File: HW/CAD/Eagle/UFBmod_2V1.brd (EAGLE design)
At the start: 98.4 x 89.5 mm, 197 parts, among them T0551 MMBT2222, U0501 MIDAS_MCCOG21605B6W-FPTLWI, U0601 MAX5217, U0701 AT86RF215-ZU, U0711 ASVTX-13-D-26.000MHZ-I05-T, U0811 PE4259, U0821 RFX1010, U0881 B39871B3440U410, U0911 FT232HL, U1101 TPS53353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

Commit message: HW_2V0 - CAD/Eagle - USB ETH and RX/TX imp lines routed
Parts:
- moved L0821 1.59 mm to (16.2, 67.3), turned to 180 degrees
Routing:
- net FPGA_ETH_RD_P: track 41.1 -> 46.7 mm, vias 3 -> 1
- net FPGA_ETH_RD_N: track 40.4 -> 45.7 mm, vias 3 -> 1
- net USB_D_P: track 38.5 -> 36.9 mm
- net ANT24: track 6.84 -> 7.79 mm, vias 0 -> 1
- net USB_D_N: track 38.6 -> 37.7 mm
- net FE09_ANT: track 4.46 -> 5.26 mm
- net FPGA_ETH_TD_P: track 41.5 -> 42.1 mm, vias 3 -> 1
- net FPGA_ETH_TD_N: track 41.1 -> 41.5 mm, vias 3 -> 1
- added copper zone on layer 1, net TRX_AVSS
- added copper zone on layer 3, net TRX_AVSS

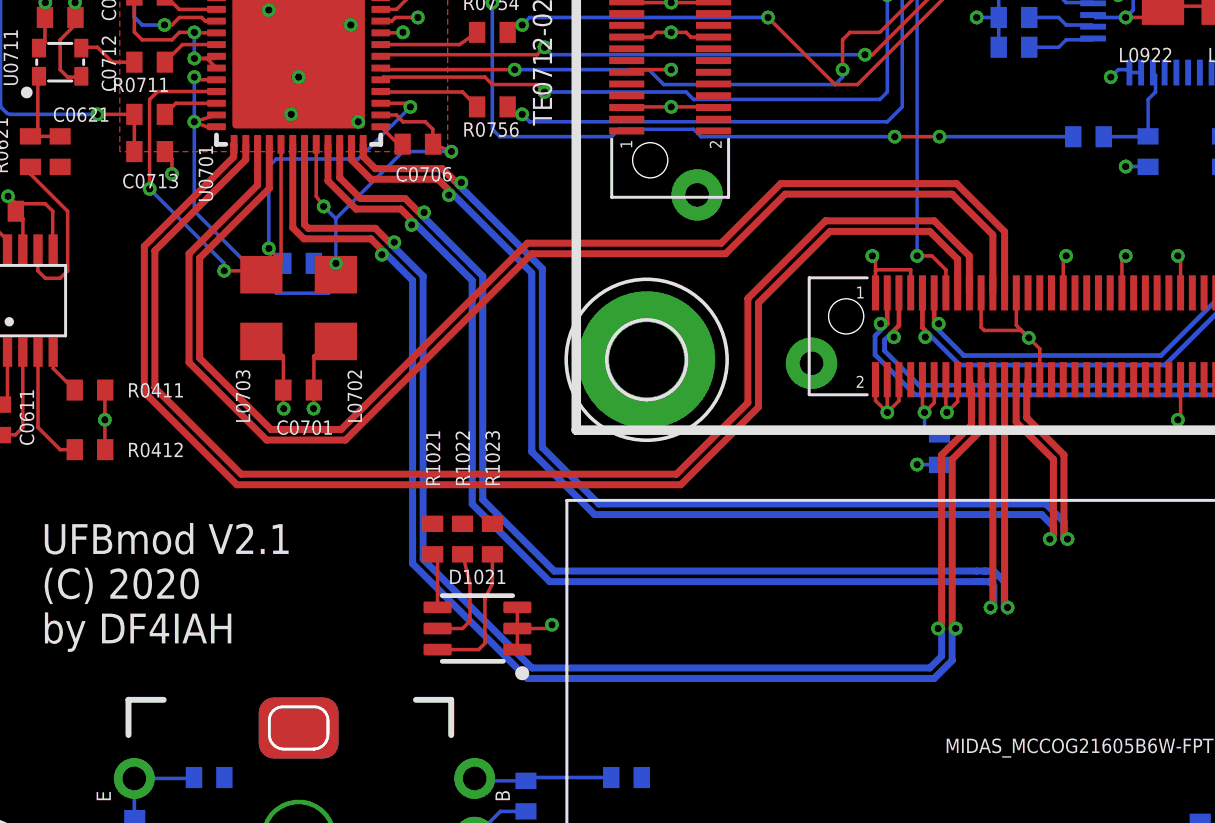
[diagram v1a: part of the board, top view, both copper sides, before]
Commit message: HW_2V0 - CAD/Eagle - LVDS imp lines routed
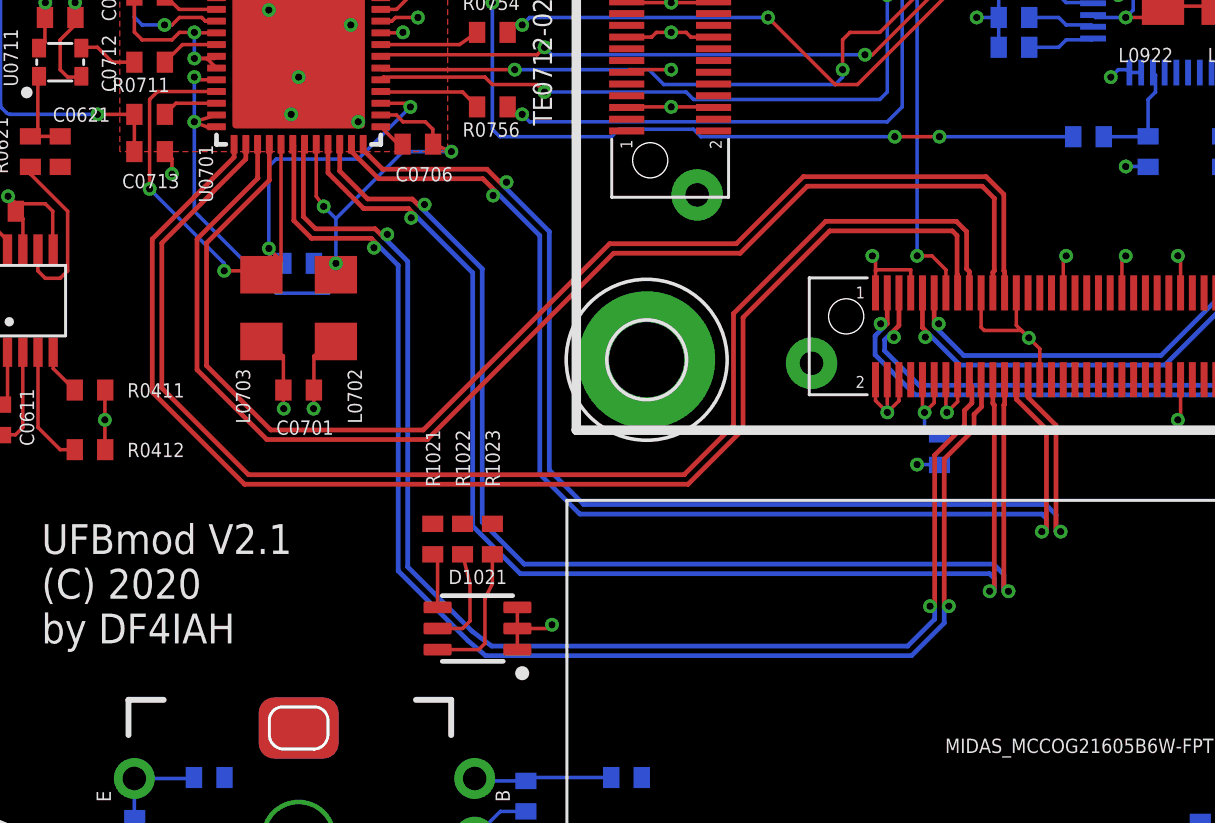
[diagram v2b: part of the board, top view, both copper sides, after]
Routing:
- net TRX_RXD09_N: track 60.1 -> 58.6 mm
- net TRX_RXD09_P: track 58.6 -> 57.3 mm
- net TRX_TXD_N: track 53.7 -> 54.6 mm
- net TRX_TXD_P: track 53.7 -> 54.6 mm
- net TRX_RXD24_N: track 50.1 -> 50.7 mm
- net TRX_RXD24_P: track 50.1 -> 50.6 mm

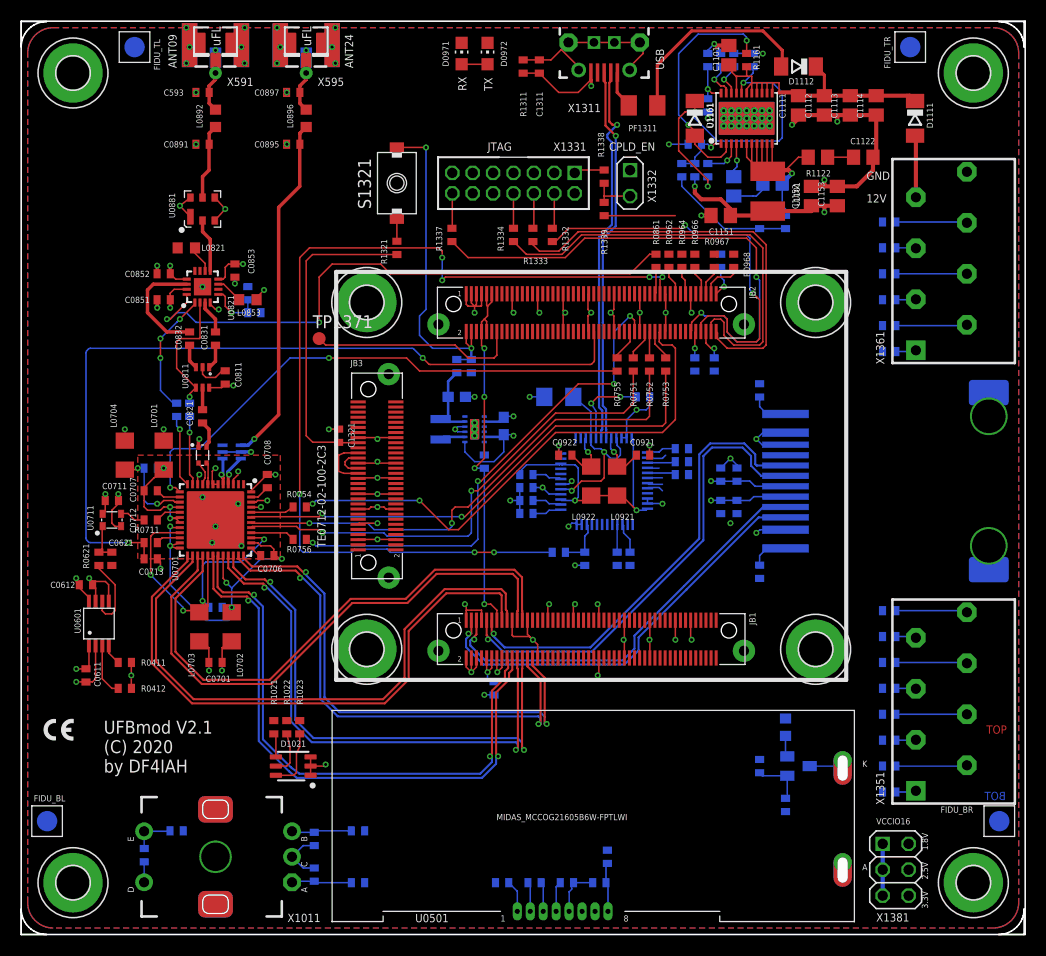
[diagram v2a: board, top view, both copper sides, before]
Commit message: HW_2V1 - CAD/Eagle - multiple nets routed
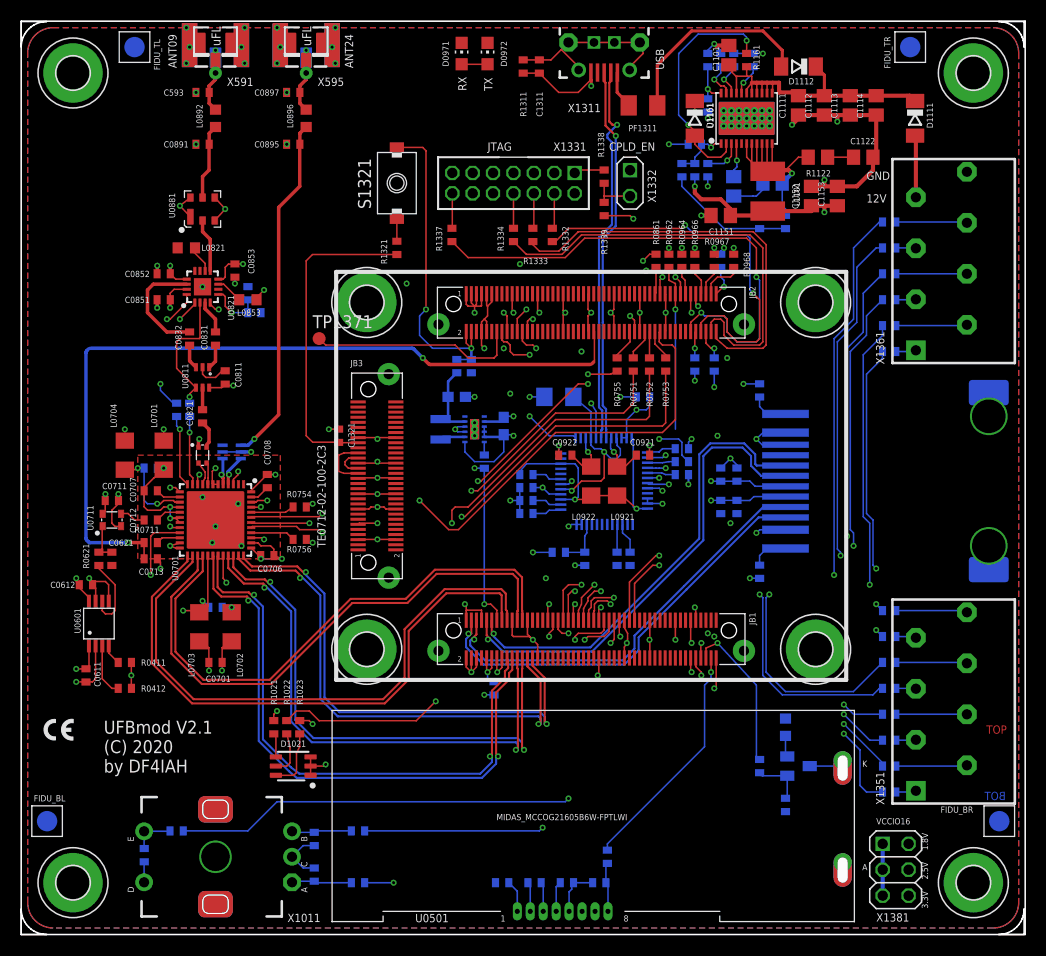
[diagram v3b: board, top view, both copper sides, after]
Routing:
- net BOARD_ROTENC_PUSH: track 0.00 -> 89.7 mm, vias 0 -> 2
- net FPGA_B16_L9_N: track 0.00 -> 69.5 mm, vias 0 -> 2
- net BOARD_ROTENC_I: track 0.00 -> 68.8 mm, vias 0 -> 2
- net BOARD_ROTENC_Q: track 0.00 -> 68.5 mm, vias 0 -> 2
- net FPGA_B16_L9_P: track 0.00 -> 64.9 mm, vias 0 -> 2
- net FPGA_B16_L11_N: track 0.00 -> 61.2 mm, vias 0 -> 2
- net FPGA_B16_L7_N: track 0.00 -> 59.5 mm, vias 0 -> 3
- net FPGA_B16_L11_P: track 0.00 -> 58.5 mm, vias 0 -> 2
- net FPGA_B16_L7_P: track 0.00 -> 56.2 mm, vias 0 -> 3
- net FPGA_ETH_DA_Y: track 0.00 -> 48.8 mm, vias 0 -> 3
- net FPGA_LED_RGB_GREEN: track 0.00 -> 46.7 mm, vias 0 -> 2
- net FPGA_LED_RGB_BLUE: track 0.00 -> 46.1 mm, vias 0 -> 2
- net FPGA_LED_RGB_RED: track 0.00 -> 46.0 mm, vias 0 -> 2
- net FPGA_JTAGEN: track 6.97 -> 51.8 mm, vias 0 -> 2
- net FPGA_B16_L19_N: track 0.00 -> 43.3 mm, vias 0 -> 2
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
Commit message: HW_2V1 - CAD/Eagle - initial routing done, ERC and DRC to follow
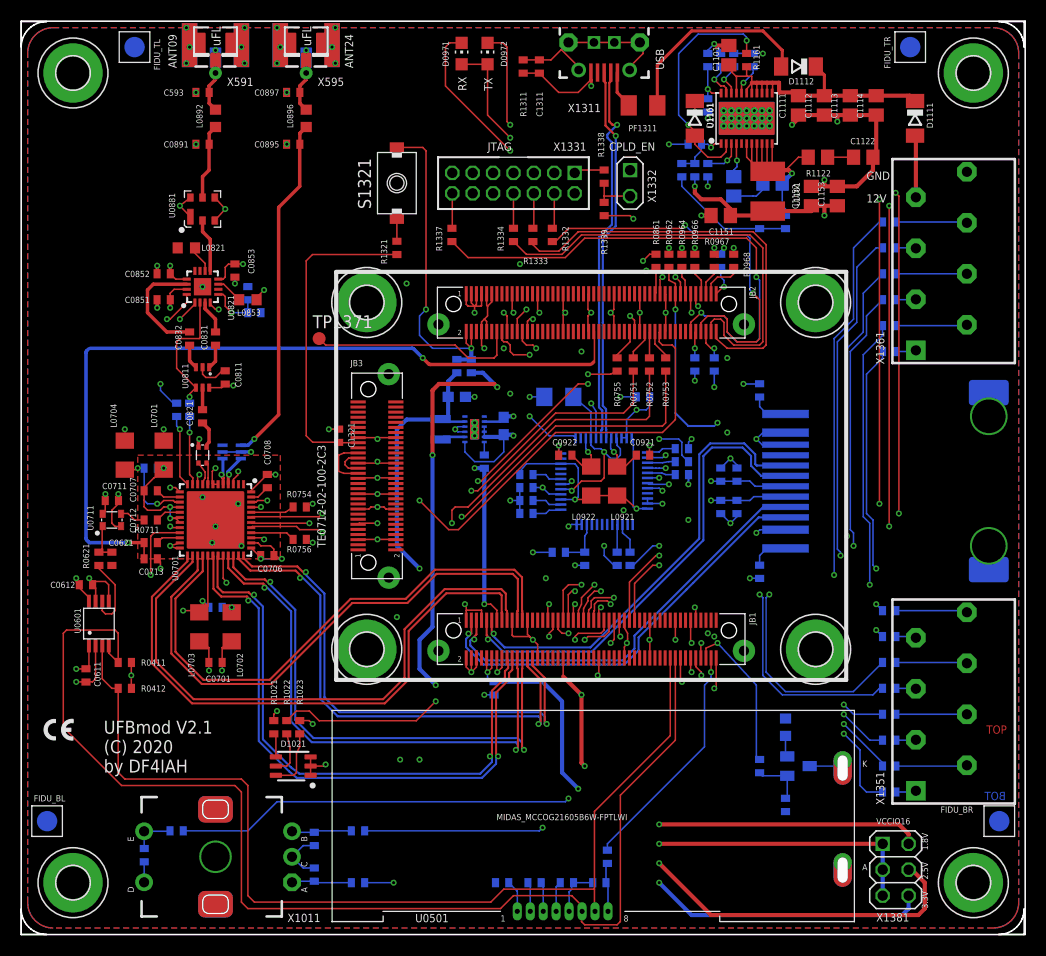
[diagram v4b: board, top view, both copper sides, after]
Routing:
- net BOARD_SDA: track 2.04 -> 119.0 mm
- net FT_TXLED_D: track 0.00 -> 115.7 mm, vias 0 -> 4
- net FT_RXLED_D: track 0.00 -> 113.3 mm, vias 0 -> 4
- net FT_VCCD: track 28.7 -> 130.4 mm, vias 2 -> 5
- net U1V8: track 0.00 -> 101.6 mm, vias 0 -> 6
- net +2V5: track 8.26 -> 107.0 mm, vias 0 -> 3
- net BOARD_SCL: track 5.21 -> 100.2 mm
- net U3V3: track 37.3 -> 118.7 mm, vias 3 -> 6
- net VCCIO16: track 9.47 -> 58.2 mm, vias 1 -> 3
- net FPGA_UART0_TXD: track 16.3 -> 58.7 mm, vias 1 -> 5
- net GND: track 237.8 -> 240.4 mm
- net FPGA_UART0_RXD: track 23.1 -> 24.7 mm

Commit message: HW_2V1 - CAD/Eagle - ERC done
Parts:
- added R0203: 10kR, df4iah_rcl:R0402
- added TP_EN1, TP_MODE, TP_PGOOD, TP_RESIN, TP_RFX_DET, TP_TXDEN: TPB1,27, df4iah_connector:B1,27
- J1411: value (none) -> ABRACON_ARJE-0034
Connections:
- new net FPGA_EN1: JB1.27, TP_EN1.TP
- new net FPGA_MODE: JB1.31, TP_MODE.TP
- new net PGOOD: JB1.29, TP_PGOOD.TP
- new net RESIN: JB2.17, R0203.1, TP_RESIN.TP
- net +3V3: now also R0203.2
- net FPGA_RFX_DET: now also TP_RFX_DET.TP
- net FT_TXDEN: now also TP_TXDEN.TP
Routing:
- net FPGA_MODE: track 0.00 -> 35.2 mm, vias 0 -> 2
- net PGOOD: track 0.00 -> 28.5 mm, vias 0 -> 2
- net FT_TXDEN: track 0.00 -> 25.7 mm, vias 0 -> 1
- net FPGA_EN1: track 0.00 -> 25.3 mm, vias 0 -> 2
- net RESIN: track 0.00 -> 4.49 mm
- net FPGA_RFX_DET: track 0.00 -> 2.97 mm, vias 0 -> 1
- net +3V3: track 95.5 -> 97.8 mm
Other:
- board text added: "TP EN1"
- board text added: "TP MODE"
- board text added: "TP PGOOD"
- board text added: "TP TXDEN"

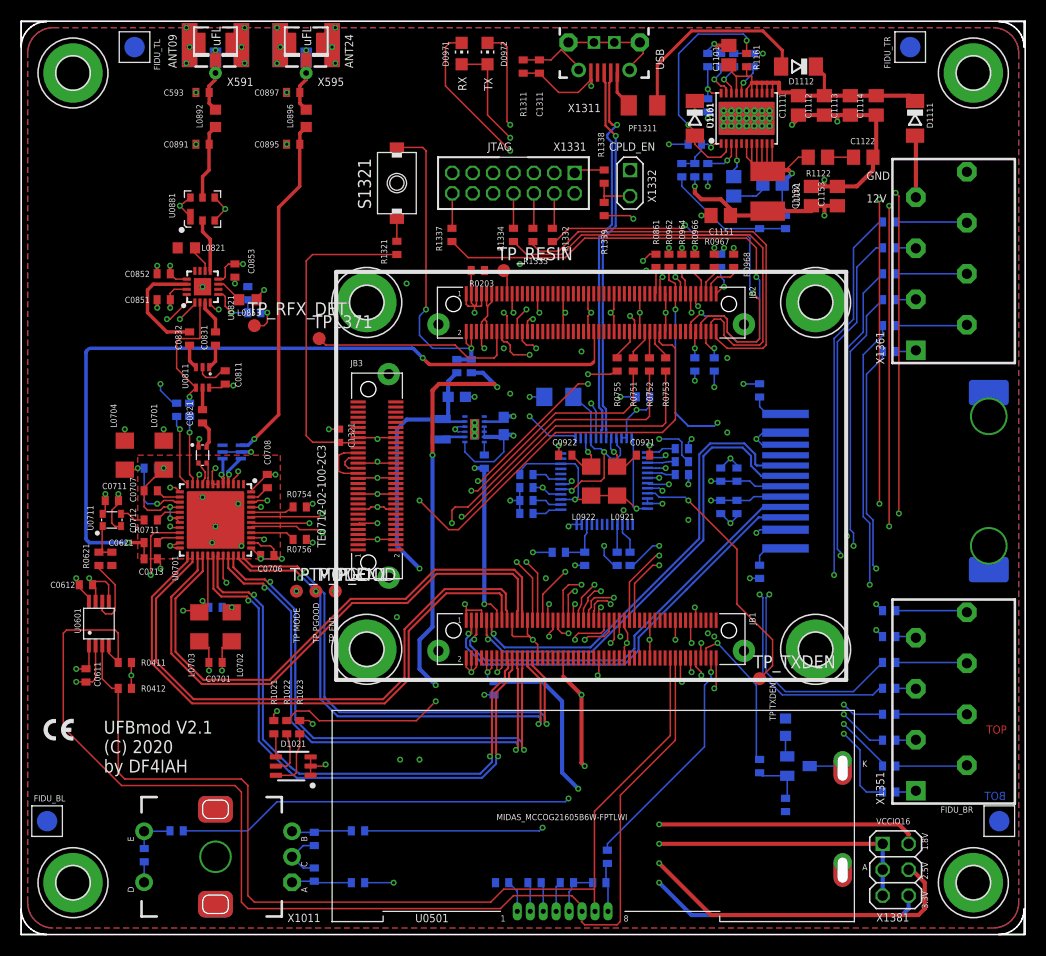
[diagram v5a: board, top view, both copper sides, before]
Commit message: HW_2V1 - CAD/Eagle - DRC work-of-the-day
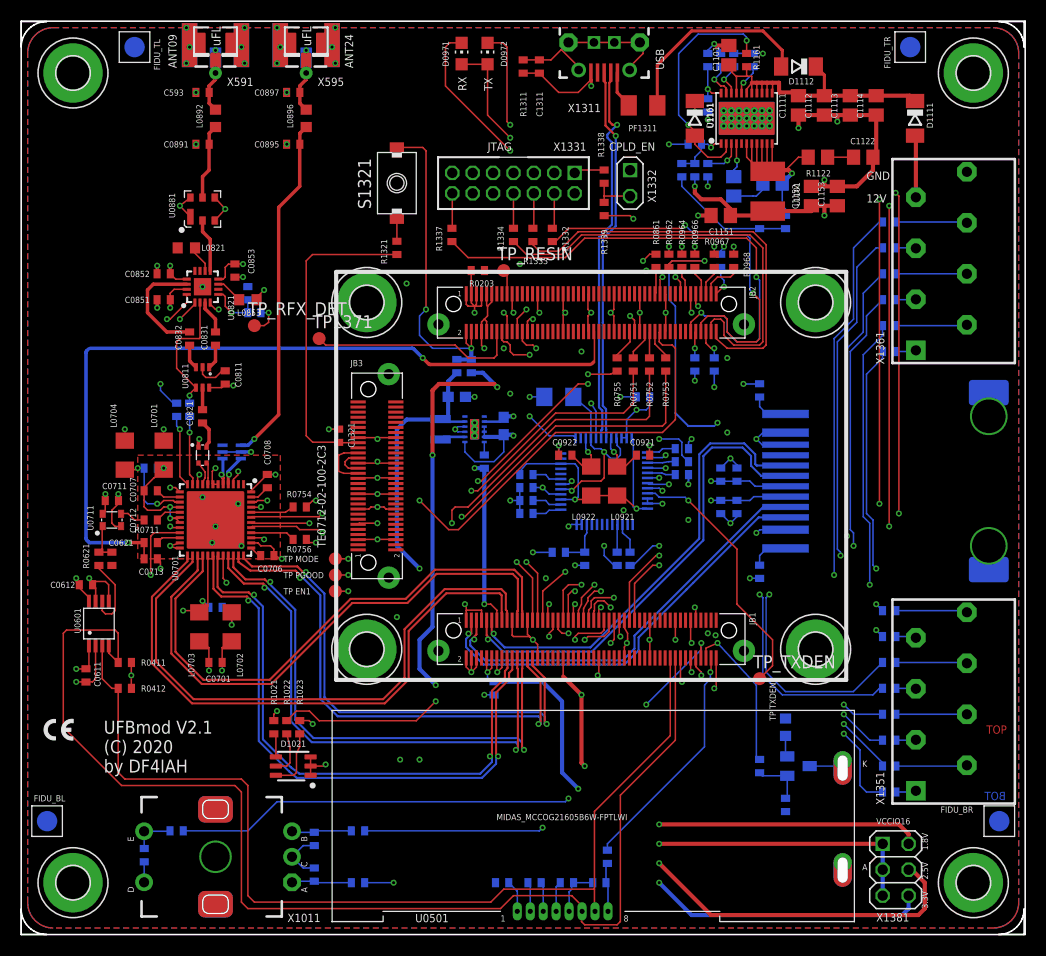
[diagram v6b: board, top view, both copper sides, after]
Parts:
- removed TP_MODE, TP_PGOOD: TPB1,27, df4iah_connector:B1,27
- added FPGA_MODE, PGOOD: TPB1,27, df4iah_connector:B1,27
- renumbered TP_EN1 to FPGA_EN1
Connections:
- net FPGA_MODE: now also FPGA_MODE.TP; no longer TP_MODE.TP
- net PGOOD: now also PGOOD.TP; no longer TP_PGOOD.TP
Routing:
- net FPGA_UART0_TXD: track 58.7 -> 66.5 mm
- net TRX_DVSS: track 34.1 -> 37.0 mm, vias 6 -> 5
- net FPGA_EN1: track 25.3 -> 26.7 mm
- net FPGA_MODE: track 35.2 -> 33.9 mm
- net FPGA_LED_RGB_GREEN: vias 2 -> 3

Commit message: HW_2V1 - CAD/Eagle - DRC complete
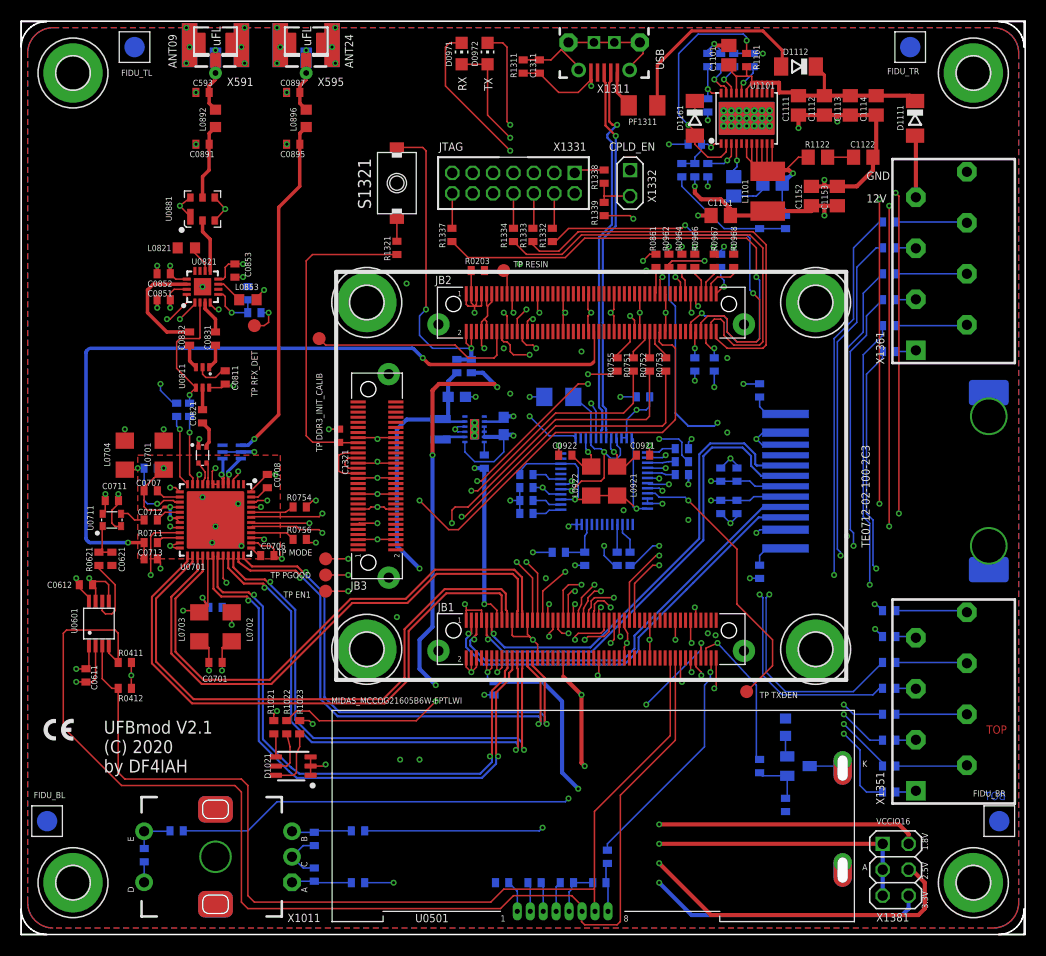
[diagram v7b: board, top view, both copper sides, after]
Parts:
- moved TP_TXDEN 1.80 mm to (71.1, 23.8)
- moved FPGA_EN1 0.95 mm to (29.8, 33.7)
- moved FPGA_MODE 0.95 mm to (29.8, 36.8)
- moved PGOOD 0.95 mm to (29.8, 35.2)
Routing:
- net FT_TXDEN: track 25.7 -> 27.5 mm
- net PGOOD: track 28.5 -> 29.5 mm
- net FPGA_MODE: track 33.9 -> 34.8 mm
- net FPGA_EN1: track 26.7 -> 27.7 mm
- net TRX_DEVDD: track 33.1 -> 33.8 mm
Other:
- board text added: "TP DDR3_INIT_CALIB"
- board text added: "TP RESIN"
- board text added: "TP RFX_DET"
- board text removed: "WDG20..WDG24"
